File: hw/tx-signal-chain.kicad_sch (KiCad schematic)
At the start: 8 parts, among them Q1101 2N7002, Q1102 NVMFD5C466NLET1G, Q403 IRFP250NPBF, U401 UCC27511ADBV

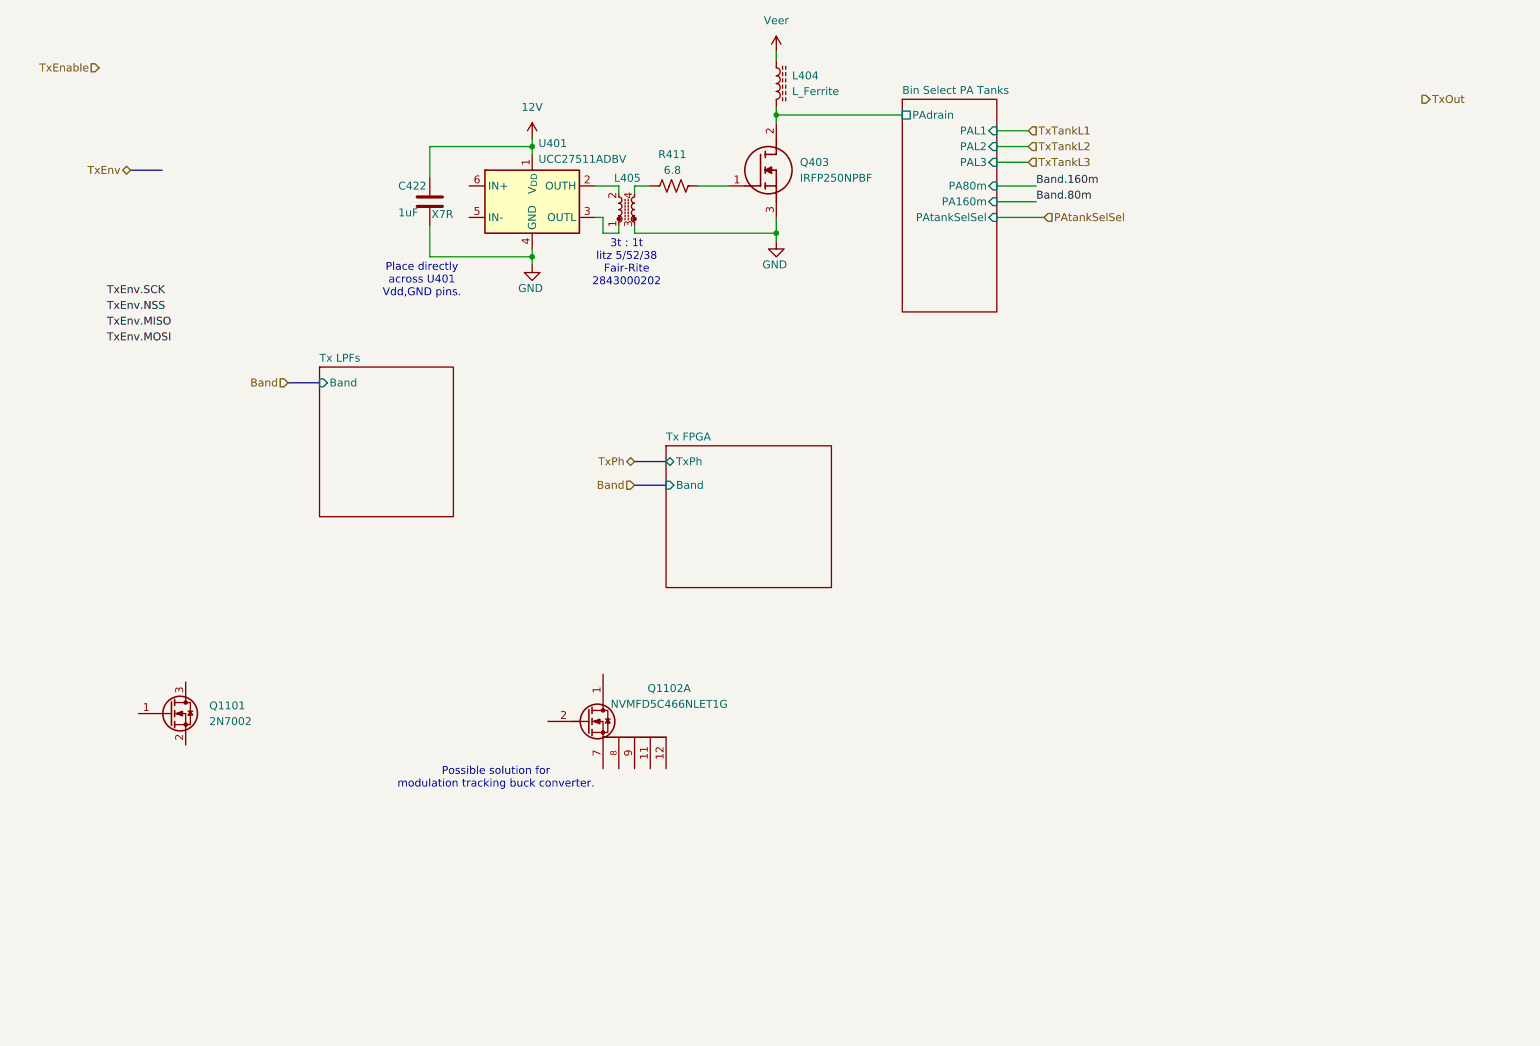
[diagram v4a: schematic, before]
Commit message: Tx LPF and its selection is pretty much done. Fix some OCD. Start to describe the design and construction.
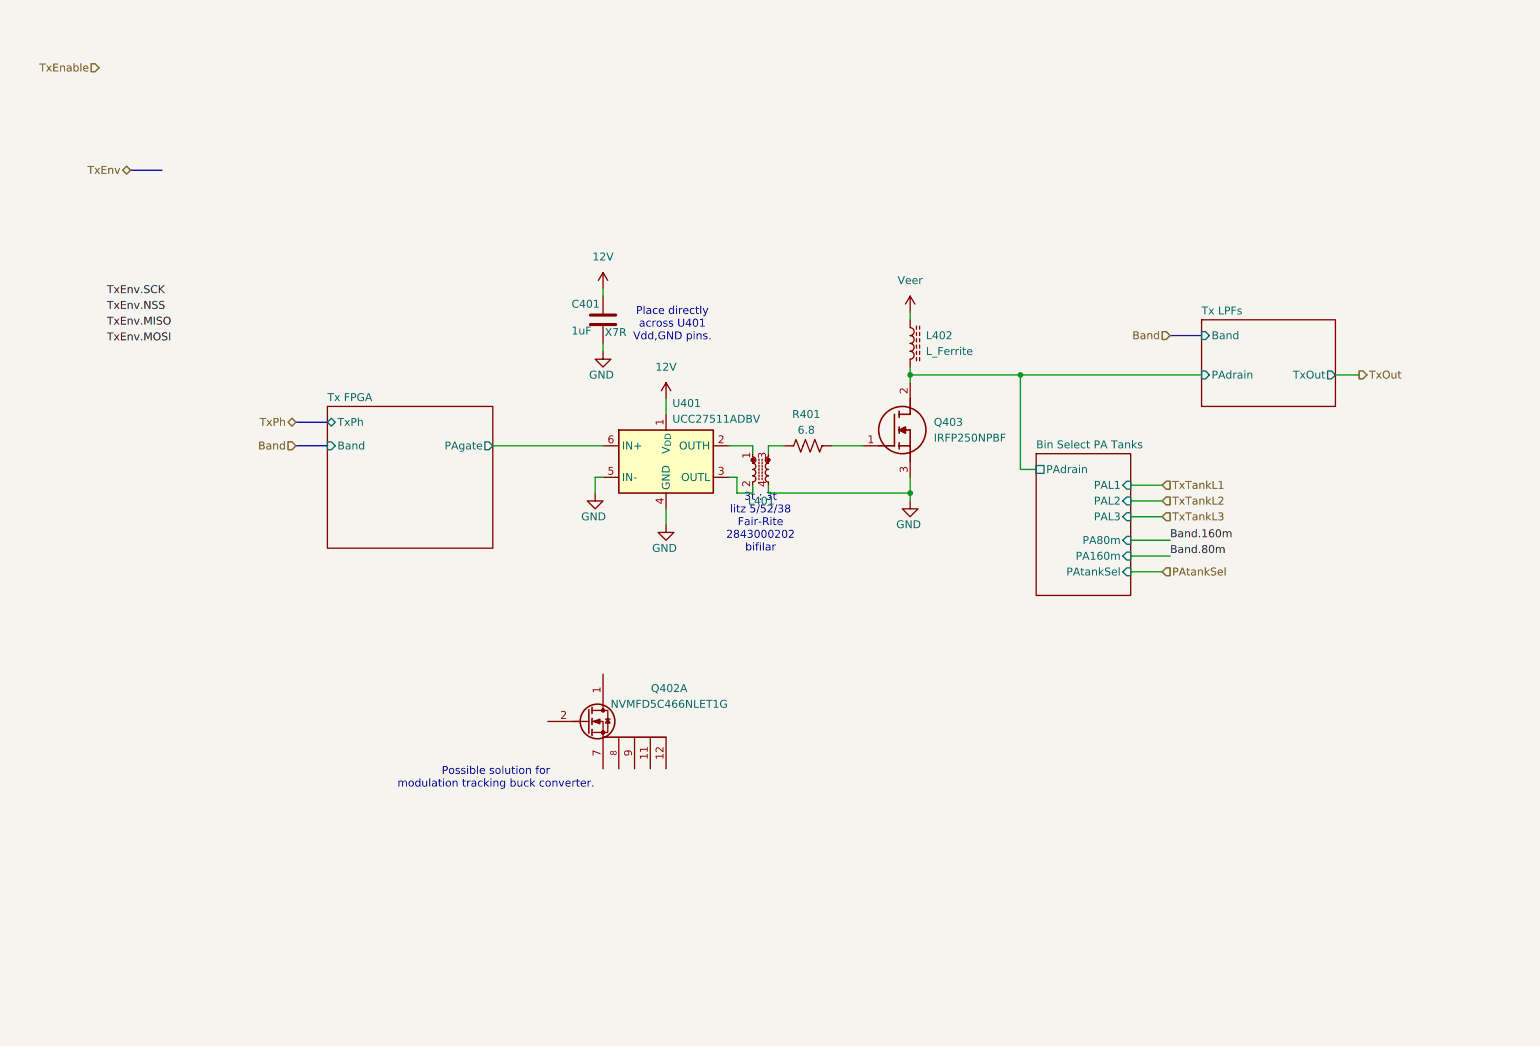
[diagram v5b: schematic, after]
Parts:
- removed Q1101: 2N7002, Package_TO_SOT_SMD:SOT-23, symbol Transistor_FET:2N7002
- renumbered C422 to C401, L405 to L401, L404 to L402, Q1102 to Q402, R411 to R401
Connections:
- net GND: now also L401.4, U401.5 (IN-); no longer L401.3
- net at U401.2 (OUTH): now also L401.1; no longer L401.2
- net at U401.3 (OUTL): now also L401.2; no longer L401.1
- net Tx FPGA/PAgate: now reaches U401.6 (IN+)
- net at R401.1: now also L401.3; no longer L401.4
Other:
- sheet Bin Select PA Tanks ports: added PAtankSel; removed PAtankSelSel
- sheet Tx FPGA ports: added PAgate; removed none
- sheet Tx LPFs ports: added PAdrain, TxOut; removed none
- note added: "3t : 3t litz 5/52/38 Fair-Rite 2843000202 bifilar"
- note removed: "3t : 1t litz 5/52/38 Fair-Rite 2843000202"
- moved on the sheet: C401, L401, L402, Q403, R401, U401

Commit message: Checkpoint
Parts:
- removed L402: L_Ferrite, symbol Device:L_Ferrite
- removed Q402: NVMFD5C466NLET1G, NVMFD030N06C, symbol NVMFD5C466NLET1G:NVMFD5C466NLET1G
- added C402: 10uF 250V, symbol Device:C
- added C403: 0.1uF 250V, symbol Device:C
- added R402: 500k, symbol Device:R_US
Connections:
- net PA Tanks/PAdrain: now also C403.2; no longer Q403.2 (D)
- net GND: now also C402.2
- net TxOut: now also R402.1
- net Veer: now also Q403.2 (D), C402.1, C403.1
- new net TxSample: R402.2
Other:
- sheet Bin Select PA Tanks renamed PA Tanks
- sheet PA Tanks ports: added TxEnable, TxRelay; removed none
- sheet Tx FPGA ports: added RxPh0, RxPh1, STM32clock; removed none
- note added: "Place as close as possible to MOSFET."
- note removed: "Possible solution for modulation tracking buck converter."

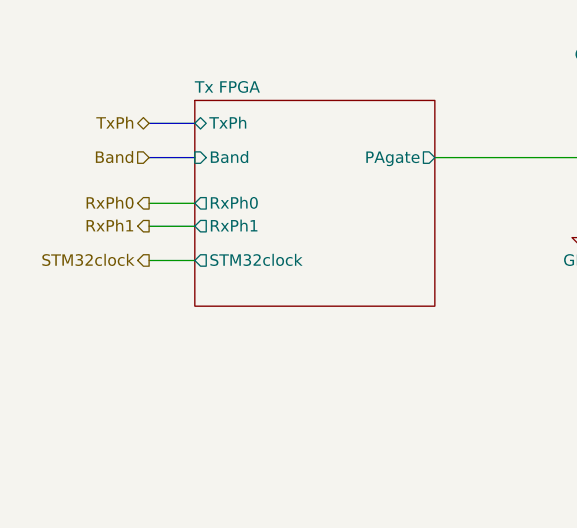
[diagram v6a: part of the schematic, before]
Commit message: Starting FPGA power sequencing.
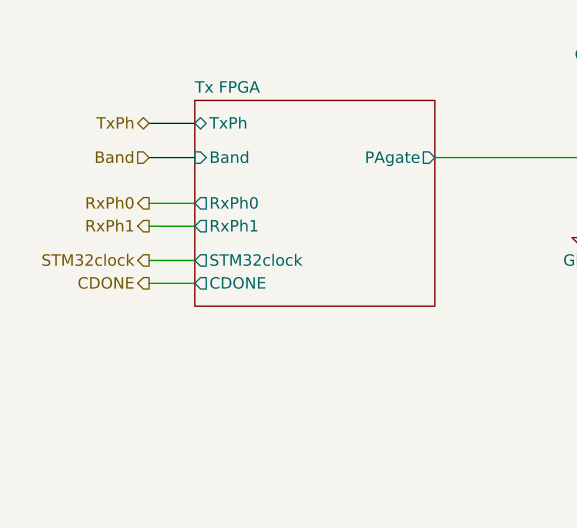
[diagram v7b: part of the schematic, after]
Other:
- sheet Tx FPGA ports: added CDONE; removed none
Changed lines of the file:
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@@
+		)
+	)
+	(wire
+		(pts
+			(xy 60.96 99.06) (xy 66.04 99.06)
+		)
+		(stroke
+			(width 0)
+			(type default)
 		)
 	)
@@
 		(shape bidirectional)
 		(at 60.96 81.28 180)
+		(effects
+			(font
+				(size 1.27 1.27)
+			)
+			(justify right)
+		)
+	)
+	(hierarchical_label "CDONE"
+		(shape output)
+		(at 60.96 99.06 180)
 		(effects
 			(font
@@
 			(effects
 				(font
+					(size 1.27 1.27)
+				)
+				(justify left)
+			)
+		)
+		(pin "CDONE" output
+			(at 66.04 99.06 180)
+			(effects
+				(font

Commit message: Veer buck/boost schematic now seems done.
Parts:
- renumbered Q403 to Q401
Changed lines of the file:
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@@
 		(dnp no)
 		(fields_autoplaced yes)
-		(property "Reference" "#PWR0405"
+		(property "Reference" "#PWR0402"
 			(at 110.49 63.5 0)
 			(effects
@@
 			(project "USB-SSB-txcvr"
 				(path "/8ae46c04-d01a-4756-8774-512b694bfaff/2406d03c-531b-4eaf-8b4b-4b266b9d0f2b"
-					(reference "#PWR0405")
+					(reference "#PWR0402")
 					(unit 1)
 				)
@@
 		(dnp no)
 		(fields_autoplaced yes)
-		(property "Reference" "#PWR0403"
+		(property "Reference" "#PWR0407"
 			(at 160.02 66.04 0)
 			(effects
@@
 			(project "USB-SSB-txcvr"
 				(path "/8ae46c04-d01a-4756-8774-512b694bfaff/2406d03c-531b-4eaf-8b4b-4b266b9d0f2b"
-					(reference "#PWR0403")
+					(reference "#PWR0407")
 					(unit 1)
 				)
@@
 		(on_board yes)
 		(dnp no)
-		(property "Reference" "#PWR0408"
+		(property "Reference" "#PWR0406"
 			(at 153.67 81.28 0)
 			(effects
@@
 			(project "USB-SSB-txcvr"
 				(path "/8ae46c04-d01a-4756-8774-512b694bfaff/2406d03c-531b-4eaf-8b4b-4b266b9d0f2b"
-					(reference "#PWR0408")
+					(reference "#PWR0406")
 					(unit 1)
 				)
@@
 		(on_board yes)
 		(dnp no)
-		(property "Reference" "#PWR0404"
+		(property "Reference" "#PWR0408"
 			(at 160.02 100.33 0)
 			(effects
@@
 			(project "USB-SSB-txcvr"
 				(path "/8ae46c04-d01a-4756-8774-512b694bfaff/2406d03c-531b-4eaf-8b4b-4b266b9d0f2b"
-					(reference "#PWR0404")
+					(reference "#PWR0408")
 					(unit 1)
 				)
@@
 		(dnp no)
 		(fields_autoplaced yes)
-		(property "Reference" "#PWR0401"
+		(property "Reference" "#PWR0404"
 			(at 120.65 81.28 0)
 			(effects
@@
 			(project "USB-SSB-txcvr"
 				(path "/8ae46c04-d01a-4756-8774-512b694bfaff/2406d03c-531b-4eaf-8b4b-4b266b9d0f2b"
-					(reference "#PWR0401")
+					(reference "#PWR0404")
 					(unit 1)
 				)
@@
 		(on_board yes)
 		(dnp no)
-		(property "Reference" "#PWR0402"
+		(property "Reference" "#PWR0405"
 			(at 120.65 104.14 0)
 			(effects
@@
 			(project "USB-SSB-txcvr"
 				(path "/8ae46c04-d01a-4756-8774-512b694bfaff/2406d03c-531b-4eaf-8b4b-4b266b9d0f2b"
-					(reference "#PWR0402")
+					(reference "#PWR0405")
 					(unit 1)
 				)
@@
 		(dnp no)
 		(fields_autoplaced yes)
-		(property "Reference" "Q403"
+		(property "Reference" "Q401"
 			(at 163.83 81.2799 0)
 			(effects
@@
 			(project ""
 				(path "/8ae46c04-d01a-4756-8774-512b694bfaff/2406d03c-531b-4eaf-8b4b-4b266b9d0f2b"
-					(reference "Q403")
+					(reference "Q401")
 					(unit 1)
 				)
@@
 		(on_board yes)
 		(dnp no)
-		(property "Reference" "#PWR0407"
+		(property "Reference" "#PWR0401"
 			(at 109.22 99.06 0)
 			(effects
@@
 			(project "USB-SSB-txcvr"
 				(path "/8ae46c04-d01a-4756-8774-512b694bfaff/2406d03c-531b-4eaf-8b4b-4b266b9d0f2b"
-					(reference "#PWR0407")
+					(reference "#PWR0401")
 					(unit 1)
 				)
@@
 		(on_board yes)
 		(dnp no)
-		(property "Reference" "#PWR0406"
+		(property "Reference" "#PWR0403"
 			(at 110.49 76.2 0)
 			(effects
@@
 			(project "USB-SSB-txcvr"
 				(path "/8ae46c04-d01a-4756-8774-512b694bfaff/2406d03c-531b-4eaf-8b4b-4b266b9d0f2b"
-					(reference "#PWR0406")
-					(unit 1)
-				)
+					(reference "#PWR0403")
+					(unit 1)
+				)
